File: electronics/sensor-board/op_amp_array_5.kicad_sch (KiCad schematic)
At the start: 21 parts

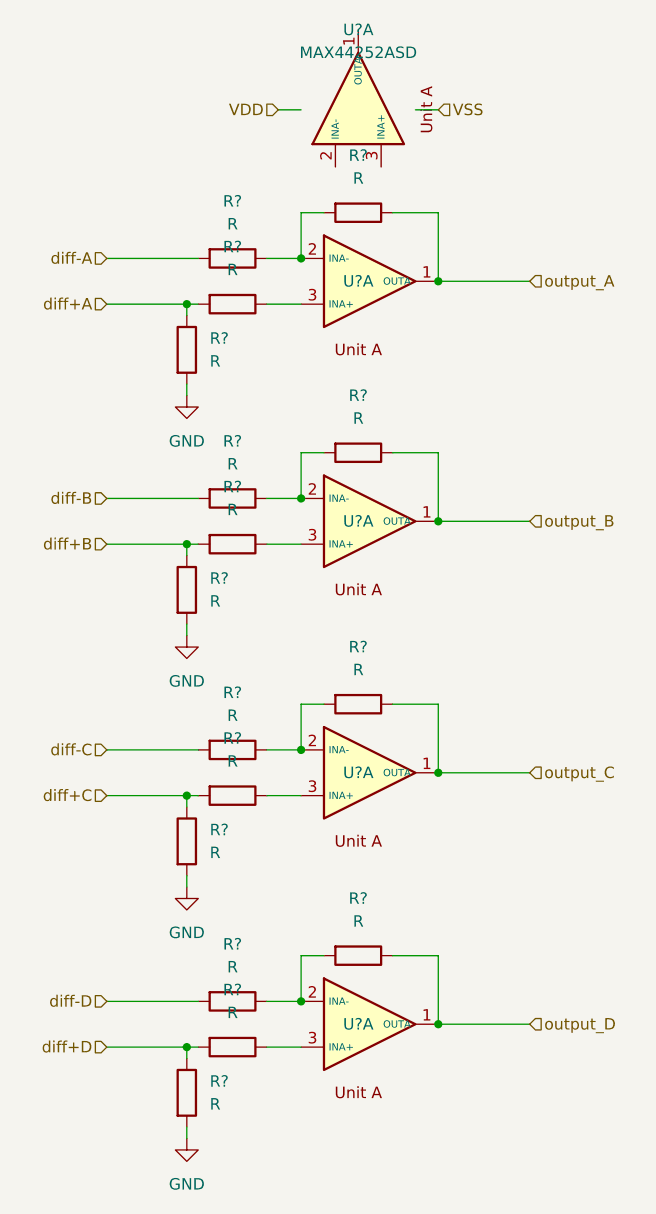
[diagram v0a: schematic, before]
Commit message: sensor-board layout edit
op amp subunits added
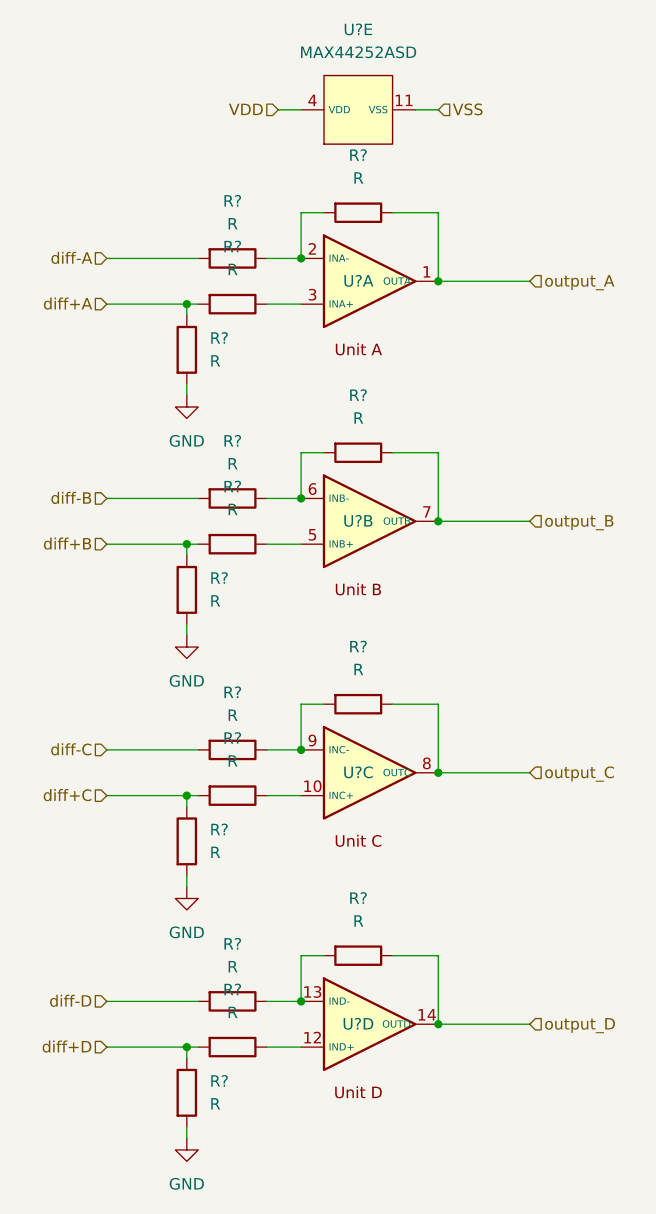
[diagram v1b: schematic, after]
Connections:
- net VDD: now also U?.4 (VDD)
- net VSS: now also U?.11 (VSS)
- net output_B: now also U?.7 (OUTB); no longer U?.1 (OUTA)
- net output_C: now also U?.8 (OUTC); no longer U?.1 (OUTA)
- net output_D: now also U?.14 (OUTD); no longer U?.1 (OUTA)
- net at R?.1, R?.2: now also U?.9 (INC-); no longer U?.2 (INA-)
- net at R?.1: now also U?.10 (INC+); no longer U?.3 (INA+)
- net at R?.1, R?.2: now also U?.13 (IND-); no longer U?.2 (INA-)
- net at R?.1: now also U?.5 (INB+); no longer U?.3 (INA+)
- net at R?.1, R?.2: now also U?.6 (INB-); no longer U?.2 (INA-)
- net at R?.1: now also U?.12 (IND+); no longer U?.3 (INA+)
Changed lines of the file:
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@@
     (effects (font (size 1.27 1.27)) (justify left))
   )
-  (symbol (lib_id "power:GND") (at 134.62 76.2 0)
+  (symbol (lib_id "power:GND") (at 134.62 76.2 0) (unit 1)
     (in_bom yes) (on_board yes) (fields_autoplaced)
     (property "Reference" "#PWR?" (id 0) (at 134.62 82.55 0)
@@
     (pin "1")
   )
-  (symbol (lib_id "power:GND") (at 134.62 102.87 0)
+  (symbol (lib_id "power:GND") (at 134.62 102.87 0) (unit 1)
     (in_bom yes) (on_board yes) (fields_autoplaced)
     (property "Reference" "#PWR?" (id 0) (at 134.62 109.22 0)
@@
     (pin "1")
   )
-  (symbol (lib_id "power:GND") (at 134.62 130.81 0)
+  (symbol (lib_id "power:GND") (at 134.62 130.81 0) (unit 1)
     (in_bom yes) (on_board yes) (fields_autoplaced)
     (property "Reference" "#PWR?" (id 0) (at 134.62 137.16 0)
@@
     (pin "1")
   )
-  (symbol (lib_id "power:GND") (at 134.62 158.75 0)
+  (symbol (lib_id "power:GND") (at 134.62 158.75 0) (unit 1)
     (in_bom yes) (on_board yes) (fields_autoplaced)
     (property "Reference" "#PWR?" (id 0) (at 134.62 165.1 0)
@@
     (pin "1")
   )
-  (symbol (lib_id "Device:R") (at 134.62 71.12 0)
+  (symbol (lib_id "Device:R") (at 134.62 71.12 0) (unit 1)
     (in_bom yes) (on_board yes) (fields_autoplaced)
     (property "Reference" "R?" (id 0) (at 137.16 69.8499 0)
@@
     (pin "2")
   )
-  (symbol (lib_id "Device:R") (at 134.62 97.79 0)
+  (symbol (lib_id "Device:R") (at 134.62 97.79 0) (unit 1)
     (in_bom yes) (on_board yes) (fields_autoplaced)
     (property "Reference" "R?" (id 0) (at 137.16 96.5199 0)
@@
     (pin "2")
   )
-  (symbol (lib_id "Device:R") (at 134.62 125.73 0)
+  (symbol (lib_id "Device:R") (at 134.62 125.73 0) (unit 1)
     (in_bom yes) (on_board yes) (fields_autoplaced)
     (property "Reference" "R?" (id 0) (at 137.16 124.4599 0)
@@
     (pin "2")
   )
-  (symbol (lib_id "Device:R") (at 134.62 153.67 0)
+  (symbol (lib_id "Device:R") (at 134.62 153.67 0) (unit 1)
     (in_bom yes) (on_board yes) (fields_autoplaced)
     (property "Reference" "R?" (id 0) (at 137.16 152.3999 0)
@@
     (pin "2")
   )
-  (symbol (lib_id "Device:R") (at 139.7 60.96 270)
+  (symbol (lib_id "Device:R") (at 139.7 60.96 270) (unit 1)
     (in_bom yes) (on_board yes) (fields_autoplaced)
     (property "Reference" "R?" (id 0) (at 139.7 54.61 90))
@@
     (pin "2")
   )
-  (symbol (lib_id "Device:R") (at 139.7 66.04 270)
+  (symbol (lib_id "Device:R") (at 139.7 66.04 270) (unit 1)
     (in_bom yes) (on_board yes) (fields_autoplaced)
     (property "Reference" "R?" (id 0) (at 139.7 59.69 90))
@@
     (pin "2")
   )
-  (symbol (lib_id "Device:R") (at 139.7 87.63 270)
+  (symbol (lib_id "Device:R") (at 139.7 87.63 270) (unit 1)
     (in_bom yes) (on_board yes) (fields_autoplaced)
     (property "Reference" "R?" (id 0) (at 139.7 81.28 90))
@@
     (pin "2")
   )
-  (symbol (lib_id "Device:R") (at 139.7 92.71 270)
+  (symbol (lib_id "Device:R") (at 139.7 92.71 270) (unit 1)
     (in_bom yes) (on_board yes) (fields_autoplaced)
     (property "Reference" "R?" (id 0) (at 139.7 86.36 90))
@@
     (pin "2")
   )
-  (symbol (lib_id "Device:R") (at 139.7 115.57 270)
+  (symbol (lib_id "Device:R") (at 139.7 115.57 270) (unit 1)
     (in_bom yes) (on_board yes) (fields_autoplaced)
     (property "Reference" "R?" (id 0) (at 139.7 109.22 90))
@@
     (pin "2")
   )
-  (symbol (lib_id "Device:R") (at 139.7 120.65 270)
+  (symbol (lib_id "Device:R") (at 139.7 120.65 270) (unit 1)
     (in_bom yes) (on_board yes) (fields_autoplaced)
     (property "Reference" "R?" (id 0) (at 139.7 114.3 90))
@@
     (pin "2")
   )
-  (symbol (lib_id "Device:R") (at 139.7 143.51 270)
+  (symbol (lib_id "Device:R") (at 139.7 143.51 270) (unit 1)
     (in_bom yes) (on_board yes) (fields_autoplaced)
     (property "Reference" "R?" (id 0) (at 139.7 137.16 90))
@@
     (pin "2")
   )
-  (symbol (lib_id "Device:R") (at 139.7 148.59 270)
+  (symbol (lib_id "Device:R") (at 139.7 148.59 270) (unit 1)
     (in_bom yes) (on_board yes) (fields_autoplaced)
     (property "Reference" "R?" (id 0) (at 139.7 142.24 90))
@@
     (pin "2")
   )
-  (symbol (lib_id "Device:R") (at 153.67 55.88 270)
+  (symbol (lib_id "Device:R") (at 153.67 55.88 270) (unit 1)
     (in_bom yes) (on_board yes) (fields_autoplaced)
     (property "Reference" "R?" (id 0) (at 153.67 49.53 90))
@@
     (pin "2")
   )
-  (symbol (lib_id "Device:R") (at 153.67 82.55 270)
+  (symbol (lib_id "Device:R") (at 153.67 82.55 270) (unit 1)
     (in_bom yes) (on_board yes) (fields_autoplaced)
     (property "Reference" "R?" (id 0) (at 153.67 76.2 90))
@@
     (pin "2")
   )
-  (symbol (lib_id "Device:R") (at 153.67 110.49 270)
+  (symbol (lib_id "Device:R") (at 153.67 110.49 270) (unit 1)
     (in_bom yes) (on_board yes) (fields_autoplaced)
     (property "Reference" "R?" (id 0) (at 153.67 104.14 90))
@@
     (pin "2")
   )
-  (symbol (lib_id "Device:R") (at 153.67 138.43 270)
+  (symbol (lib_id "Device:R") (at 153.67 138.43 270) (unit 1)
     (in_bom yes) (on_board yes) (fields_autoplaced)
     (property "Reference" "R?" (id 0) (at 153.67 132.08 90))
@@
     (pin "2")
   )
-  (symbol (lib_id "MAX44252ASD_Custom:MAX44252ASD") (at 153.67 44.45 90)
+  (symbol (lib_id "MAX44252ASD_Custom:MAX44252ASD") (at 153.67 44.45 90) (unit 5)
     (in_bom yes) (on_board yes) (fields_autoplaced)
     (property "Reference" "U?" (id 0) (at 153.67 35.56 90))
@@
     (pin "4")
   )
-  (symbol (lib_id "MAX44252ASD_Custom:MAX44252ASD") (at 153.67 63.5 0)
+  (symbol (lib_id "MAX44252ASD_Custom:MAX44252ASD") (at 153.67 63.5 0) (unit 1)
     (in_bom yes) (on_board yes)
     (property "Reference" "U?" (id 0) (at 153.67 63.5 0))
@@
     (pin "3")
   )
-  (symbol (lib_id "MAX44252ASD_Custom:MAX44252ASD") (at 153.67 90.17 0)
+  (symbol (lib_id "MAX44252ASD_Custom:MAX44252ASD") (at 153.67 90.17 0) (unit 2)
     (in_bom yes) (on_board yes)
     (property "Reference" "U?" (id 0) (at 153.67 90.17 0))
@@
     (pin "7")
   )
-  (symbol (lib_id "MAX44252ASD_Custom:MAX44252ASD") (at 153.67 118.11 0)
+  (symbol (lib_id "MAX44252ASD_Custom:MAX44252ASD") (at 153.67 118.11 0) (unit 3)
     (in_bom yes) (on_board yes)
     (property "Reference" "U?" (id 0) (at 153.67 118.11 0))
@@
     (pin "9")
   )
-  (symbol (lib_id "MAX44252ASD_Custom:MAX44252ASD") (at 153.67 146.05 0)
+  (symbol (lib_id "MAX44252ASD_Custom:MAX44252ASD") (at 153.67 146.05 0) (unit 4)
     (in_bom yes) (on_board yes)
     (property "Reference" "U?" (id 0) (at 153.67 146.05 0))
@@
     (pin "14")
   )
-  (sheet_instances
-    (path "/" (page "1"))
-  )
-  (symbol_instances
-    (path "/16f7f778-8b07-4c2f-9dca-d8f867c210ec"
-      (reference "#PWR?") (unit 1) (value "GND") (footprint "")
-    )
-    (path "/373f77a2-94d8-40e6-8241-a306c1243b73"
-      (reference "#PWR?") (unit 1) (value "GND") (footprint "")
-    )
-    (path "/ae8e89ed-fa26-4694-a091-2db224c813b2"
-      (reference "#PWR?") (unit 1) (value "GND") (footprint "")
-    )
-    (path "/f2305714-43e0-4618-af93-91d034ff0c82"
-      (reference "#PWR?") (unit 1) (value "GND") (footprint "")
-    )
-    (path "/01e516df-4b4f-4517-bde7-da6fcdde2a4f"
-      (reference "R?") (unit 1) (value "R") (footprint "")
-    )
-    (path "/1688ae91-6e8e-4120-9669-4d0ca6d76832"
-      (reference "R?") (unit 1) (value "R") (footprint "")
-    )
-    (path "/63de2aad-f668-4325-9908-db4199b6d076"
-      (reference "R?") (unit 1) (value "R") (footprint "")
-    )
-    (path "/66f12ab2-0712-4942-8e16-8a0f1bf4c07b"
-      (reference "R?") (unit 1) (value "R") (footprint "")
-    )
-    (path "/6c159cba-3c9c-4abb-99bc-a123fce1e1fc"
-      (reference "R?") (unit 1) (value "R") (footprint "")
-    )
-    (path "/6ee274f2-bc66-4374-971a-a15bf2535e46"
-      (reference "R?") (unit 1) (value "R") (footprint "")
-    )
-    (path "/8215ebe9-31ed-4618-8a03-52406b30c840"
-      (reference "R?") (unit 1) (value "R") (footprint "")
-    )
-    (path "/89011c12-e113-4f61-a4f5-ba92ed02be93"
-      (reference "R?") (unit 1) (value "R") (footprint "")
-    )
-    (path "/93925990-b11c-4796-9637-ceb6f4ca45f3"
-      (reference "R?") (unit 1) (value "R") (footprint "")
-    )
-    (path "/a2754056-98eb-4794-9dc8-9ea71be49d01"
-      (reference "R?") (unit 1) (value "R") (footprint "")
-    )
-    (path "/a967f099-2ad0-429f-b4b9-adb50aee64e3"
-      (reference "R?") (unit 1) (value "R") (footprint "")
-    )
-    (path "/aa4ac85e-2e8c-4185-828f-9b0af10cb333"
-      (reference "R?") (unit 1) (value "R") (footprint "")
-    )
-    (path "/b2c90e11-4b04-4931-a917-ad8b76b05ddc"
-      (reference "R?") (unit 1) (value "R") (footprint "")
-    )
-    (path "/ca0c5e51-abd5-49b2-bedc-9b35d2d57dc2"
-      (reference "R?") (unit 1) (value "R") (footprint "")
-    )
-    (path "/ed8062f1-ffb4-442c-b553-c5ab7c35894f"
-      (reference "R?") (unit 1) (value "R") (footprint "")
-    )
-    (path "/ee41aa7f-a8c6-45c8-8346-95e08e7fb6d4"
-      (reference "R?") (unit 1) (value "R") (footprint "")
-    )
-    (path "/73caf16e-2004-4ed9-84a2-71b072b85c09"
-      (reference "U?") (unit 1) (value "MAX44252ASD") (footprint "")
-    )
-    (path "/f40e150d-45e1-4ddc-aa0a-853395417499"
-      (reference "U?") (unit 2) (value "MAX44252ASD") (footprint "")
-    )
-    (path "/5d6bd069-7adf-4a23-bb05-0d89023d387c"
-      (reference "U?") (unit 3) (value "MAX44252ASD") (footprint "")
-    )
-    (path "/d9fd8f7c-82e3-4164-b8fd-7e7aa20a1284"
-      (reference "U?") (unit 4) (value "MAX44252ASD") (footprint "")
-    )
-    (path "/f0e8b943-1ebe-4b77-b286-184ba7c9a665"
-      (reference "U?") (unit 5) (value "MAX44252ASD") (footprint "")
-    )
-  )
 )

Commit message: sensor-board edit
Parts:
- removed R? (x16): R, symbol Device:R
- removed U? (x5): MAX44252ASD, symbol MAX44252ASD_Custom:MAX44252ASD
- added R? (x16): R, symbol Device:R
- added U? (x5): MAX44252ASD, symbol MAX44252ASD_Custom:MAX44252ASD
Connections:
- net GND: now also R?.2, R?.2, R?.2, R?.2
- net diff+A: now also R?.1, R?.2
- net diff+B: now also R?.1, R?.2
- net diff+C: now also R?.1, R?.2
- net diff+D: now also R?.1, R?.2
- net diff-A: now also R?.2
- net diff-B: now also R?.2
- net diff-C: now also R?.2
- net diff-D: now also R?.2
- net output_A: now also R?.1, U?.1 (OUTA)
- net output_B: now also R?.1, U?.1 (OUTA)
- net output_C: now also R?.1, U?.1 (OUTA)
- net output_D: now also R?.1, U?.1 (OUTA)
- new net: R?.1, R?.2, U?.2 (INA-) (x4)
- new net: R?.1, U?.3 (INA+) (x4)
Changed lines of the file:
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@@
     (effects (font (size 1.27 1.27)) (justify left))
   )
-  (symbol (lib_id "power:GND") (at 134.62 76.2 0) (unit 1)
+  (symbol (lib_id "power:GND") (at 134.62 76.2 0)
     (in_bom yes) (on_board yes) (fields_autoplaced)
     (property "Reference" "#PWR?" (id 0) (at 134.62 82.55 0)
@@
     (pin "1")
   )
-  (symbol (lib_id "power:GND") (at 134.62 102.87 0) (unit 1)
+  (symbol (lib_id "power:GND") (at 134.62 102.87 0)
     (in_bom yes) (on_board yes) (fields_autoplaced)
     (property "Reference" "#PWR?" (id 0) (at 134.62 109.22 0)
@@
     (pin "1")
   )
-  (symbol (lib_id "power:GND") (at 134.62 130.81 0) (unit 1)
+  (symbol (lib_id "power:GND") (at 134.62 130.81 0)
     (in_bom yes) (on_board yes) (fields_autoplaced)
     (property "Reference" "#PWR?" (id 0) (at 134.62 137.16 0)
@@
     (pin "1")
   )
-  (symbol (lib_id "power:GND") (at 134.62 158.75 0) (unit 1)
+  (symbol (lib_id "power:GND") (at 134.62 158.75 0)
     (in_bom yes) (on_board yes) (fields_autoplaced)
     (property "Reference" "#PWR?" (id 0) (at 134.62 165.1 0)
@@
     (pin "1")
   )
-  (symbol (lib_id "Device:R") (at 134.62 71.12 0) (unit 1)
+  (symbol (lib_id "Device:R") (at 134.62 71.12 0)
     (in_bom yes) (on_board yes) (fields_autoplaced)
     (property "Reference" "R?" (id 0) (at 137.16 69.8499 0)
@@
     (pin "2")
   )
-  (symbol (lib_id "Device:R") (at 134.62 97.79 0) (unit 1)
+  (symbol (lib_id "Device:R") (at 134.62 97.79 0)
     (in_bom yes) (on_board yes) (fields_autoplaced)
     (property "Reference" "R?" (id 0) (at 137.16 96.5199 0)
@@
     (pin "2")
   )
-  (symbol (lib_id "Device:R") (at 134.62 125.73 0) (unit 1)
+  (symbol (lib_id "Device:R") (at 134.62 125.73 0)
     (in_bom yes) (on_board yes) (fields_autoplaced)
     (property "Reference" "R?" (id 0) (at 137.16 124.4599 0)
@@
     (pin "2")
   )
-  (symbol (lib_id "Device:R") (at 134.62 153.67 0) (unit 1)
+  (symbol (lib_id "Device:R") (at 134.62 153.67 0)
     (in_bom yes) (on_board yes) (fields_autoplaced)
     (property "Reference" "R?" (id 0) (at 137.16 152.3999 0)
@@
     (pin "2")
   )
-  (symbol (lib_id "Device:R") (at 139.7 60.96 270) (unit 1)
+  (symbol (lib_id "Device:R") (at 139.7 60.96 270)
     (in_bom yes) (on_board yes) (fields_autoplaced)
     (property "Reference" "R?" (id 0) (at 139.7 54.61 90))
@@
     (pin "2")
   )
-  (symbol (lib_id "Device:R") (at 139.7 66.04 270) (unit 1)
+  (symbol (lib_id "Device:R") (at 139.7 66.04 270)
     (in_bom yes) (on_board yes) (fields_autoplaced)
     (property "Reference" "R?" (id 0) (at 139.7 59.69 90))
@@
     (pin "2")
   )
-  (symbol (lib_id "Device:R") (at 139.7 87.63 270) (unit 1)
+  (symbol (lib_id "Device:R") (at 139.7 87.63 270)
     (in_bom yes) (on_board yes) (fields_autoplaced)
     (property "Reference" "R?" (id 0) (at 139.7 81.28 90))
@@
     (pin "2")
   )
-  (symbol (lib_id "Device:R") (at 139.7 92.71 270) (unit 1)
+  (symbol (lib_id "Device:R") (at 139.7 92.71 270)
     (in_bom yes) (on_board yes) (fields_autoplaced)
     (property "Reference" "R?" (id 0) (at 139.7 86.36 90))
@@
     (pin "2")
   )
-  (symbol (lib_id "Device:R") (at 139.7 115.57 270) (unit 1)
+  (symbol (lib_id "Device:R") (at 139.7 115.57 270)
     (in_bom yes) (on_board yes) (fields_autoplaced)
     (property "Reference" "R?" (id 0) (at 139.7 109.22 90))
@@
     (pin "2")
   )
-  (symbol (lib_id "Device:R") (at 139.7 120.65 270) (unit 1)
+  (symbol (lib_id "Device:R") (at 139.7 120.65 270)
     (in_bom yes) (on_board yes) (fields_autoplaced)
     (property "Reference" "R?" (id 0) (at 139.7 114.3 90))
@@
     (pin "2")
   )
-  (symbol (lib_id "Device:R") (at 139.7 143.51 270) (unit 1)
+  (symbol (lib_id "Device:R") (at 139.7 143.51 270)
     (in_bom yes) (on_board yes) (fields_autoplaced)
     (property "Reference" "R?" (id 0) (at 139.7 137.16 90))
@@
     (pin "2")
   )
-  (symbol (lib_id "Device:R") (at 139.7 148.59 270) (unit 1)
+  (symbol (lib_id "Device:R") (at 139.7 148.59 270)
     (in_bom yes) (on_board yes) (fields_autoplaced)
     (property "Reference" "R?" (id 0) (at 139.7 142.24 90))
@@
     (pin "2")
   )
-  (symbol (lib_id "Device:R") (at 153.67 55.88 270) (unit 1)
+  (symbol (lib_id "Device:R") (at 153.67 55.88 270)
     (in_bom yes) (on_board yes) (fields_autoplaced)
     (property "Reference" "R?" (id 0) (at 153.67 49.53 90))
@@
     (pin "2")
   )
-  (symbol (lib_id "Device:R") (at 153.67 82.55 270) (unit 1)
+  (symbol (lib_id "Device:R") (at 153.67 82.55 270)
     (in_bom yes) (on_board yes) (fields_autoplaced)
     (property "Reference" "R?" (id 0) (at 153.67 76.2 90))
@@
     (pin "2")
   )
-  (symbol (lib_id "Device:R") (at 153.67 110.49 270) (unit 1)
+  (symbol (lib_id "Device:R") (at 153.67 110.49 270)
     (in_bom yes) (on_board yes) (fields_autoplaced)
     (property "Reference" "R?" (id 0) (at 153.67 104.14 90))
@@
     (pin "2")
   )
-  (symbol (lib_id "Device:R") (at 153.67 138.43 270) (unit 1)
+  (symbol (lib_id "Device:R") (at 153.67 138.43 270)
     (in_bom yes) (on_board yes) (fields_autoplaced)
     (property "Reference" "R?" (id 0) (at 153.67 132.08 90))
@@
     (pin "2")
   )
-  (symbol (lib_id "MAX44252ASD_Custom:MAX44252ASD") (at 153.67 44.45 90) (unit 5)
+  (symbol (lib_id "MAX44252ASD_Custom:MAX44252ASD") (at 153.67 44.45 90)
     (in_bom yes) (on_board yes) (fields_autoplaced)
     (property "Reference" "U?" (id 0) (at 153.67 35.56 90))
@@
     (pin "4")
   )
-  (symbol (lib_id "MAX44252ASD_Custom:MAX44252ASD") (at 153.67 63.5 0) (unit 1)
+  (symbol (lib_id "MAX44252ASD_Custom:MAX44252ASD") (at 153.67 63.5 0)
     (in_bom yes) (on_board yes)
     (property "Reference" "U?" (id 0) (at 153.67 63.5 0))
@@
     (pin "3")
   )
-  (symbol (lib_id "MAX44252ASD_Custom:MAX44252ASD") (at 153.67 90.17 0) (unit 2)
+  (symbol (lib_id "MAX44252ASD_Custom:MAX44252ASD") (at 153.67 90.17 0)
     (in_bom yes) (on_board yes)
     (property "Reference" "U?" (id 0) (at 153.67 90.17 0))
@@
     (pin "7")
   )
-  (symbol (lib_id "MAX44252ASD_Custom:MAX44252ASD") (at 153.67 118.11 0) (unit 3)
+  (symbol (lib_id "MAX44252ASD_Custom:MAX44252ASD") (at 153.67 118.11 0)
     (in_bom yes) (on_board yes)
     (property "Reference" "U?" (id 0) (at 153.67 118.11 0))
@@
     (pin "9")
   )
-  (symbol (lib_id "MAX44252ASD_Custom:MAX44252ASD") (at 153.67 146.05 0) (unit 4)
+  (symbol (lib_id "MAX44252ASD_Custom:MAX44252ASD") (at 153.67 146.05 0)
     (in_bom yes) (on_board yes)
     (property "Reference" "U?" (id 0) (at 153.67 146.05 0))
